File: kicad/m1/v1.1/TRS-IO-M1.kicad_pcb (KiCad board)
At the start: 2 copper layers, 117.5 x 104.8 mm, 26 parts, among them J1 Conn_02x20_Odd_Even, Q1 2N7000, Q2 2N7000, SW1 SW_Push, U1 HiLetgo-ESP-32S, U2 AS6C62256-PDIP, U3 MCP23S17_SP, U4 74LVC245, U5 74LVC245, U6 74LVC245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

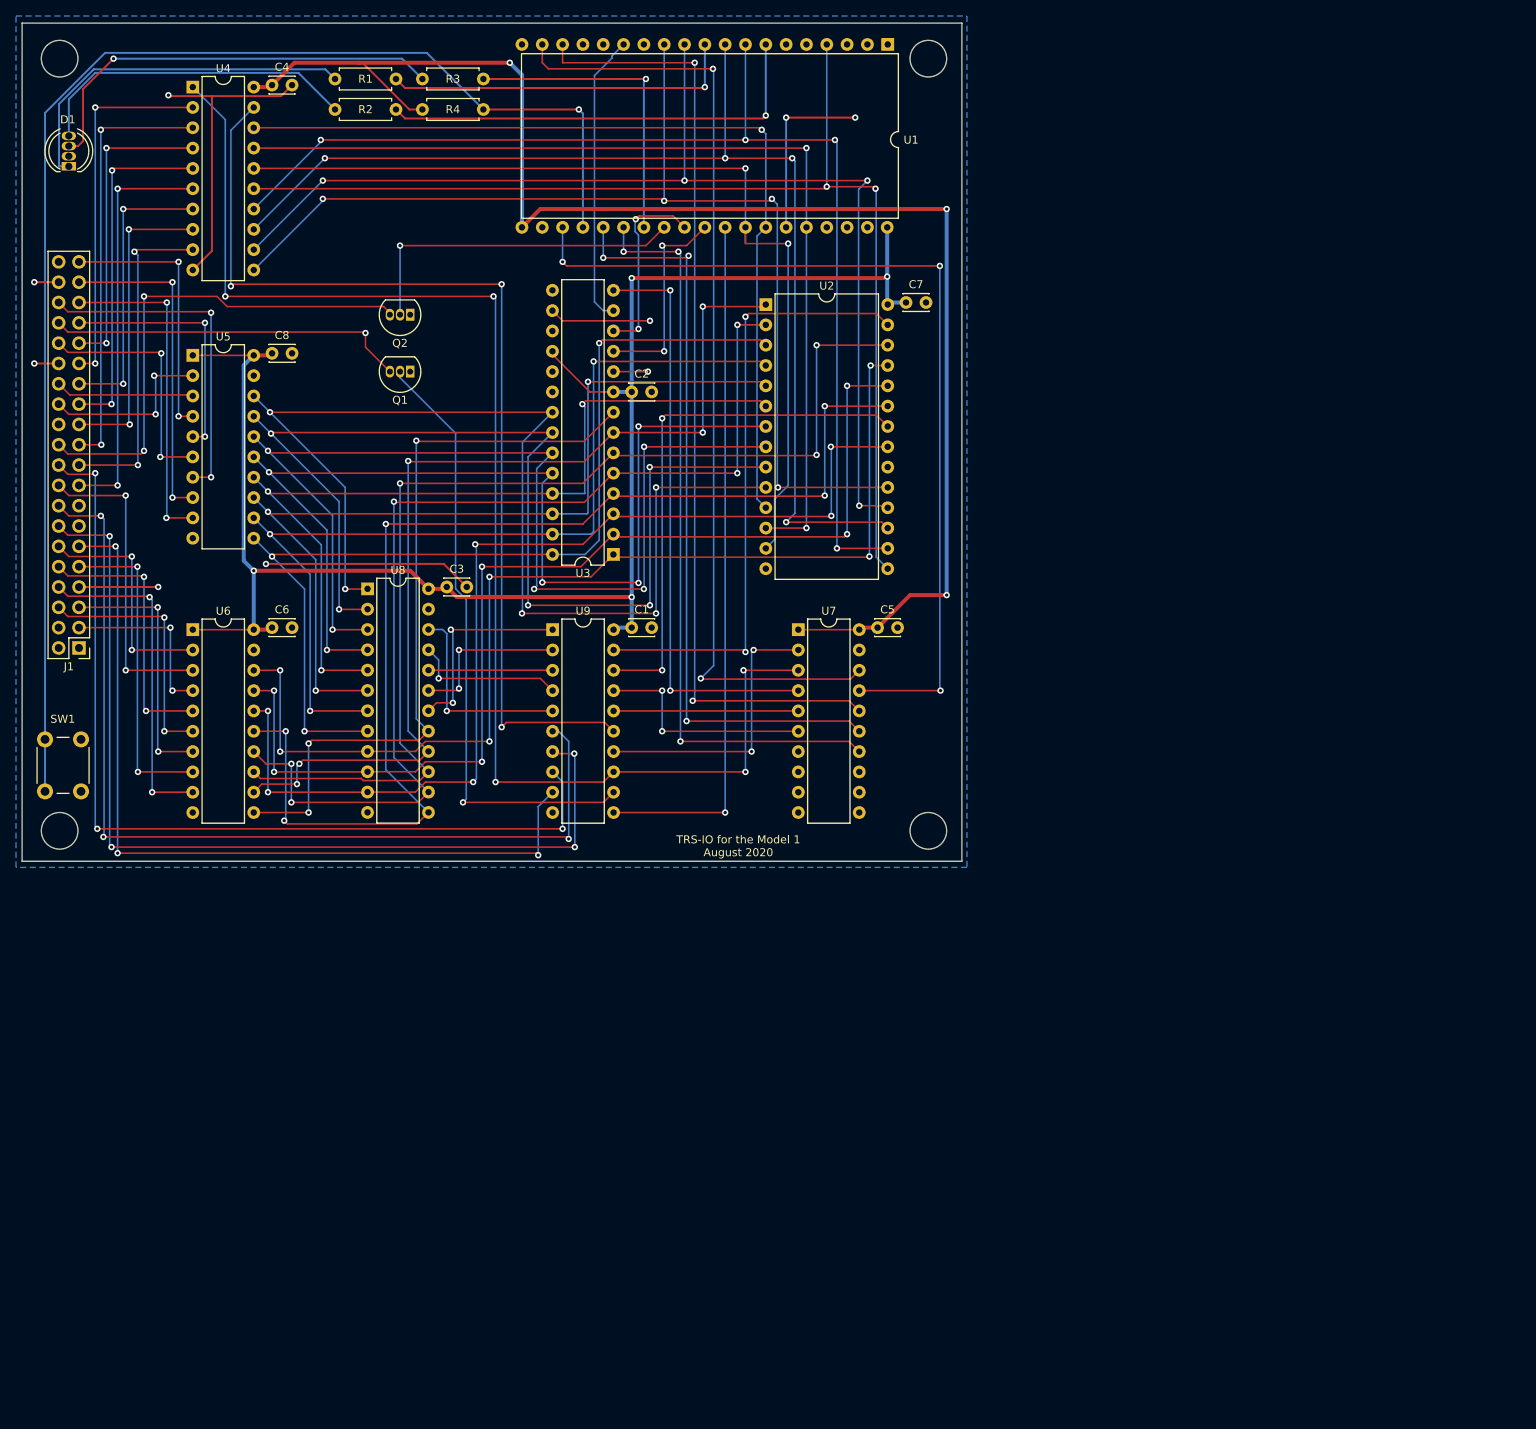
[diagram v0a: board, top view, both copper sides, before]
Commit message: Updates for TRS-IO-M1 v1.1
- Move data bus of the SRAM before the buffer
- added J2 for the edge connector
- Removed ADDR_2 and repurposed the connection for RAS*
- Move ESP_SEL_N to GPIO 27
- Move ESP_WAIT_RELEASE_N to GPIO 2
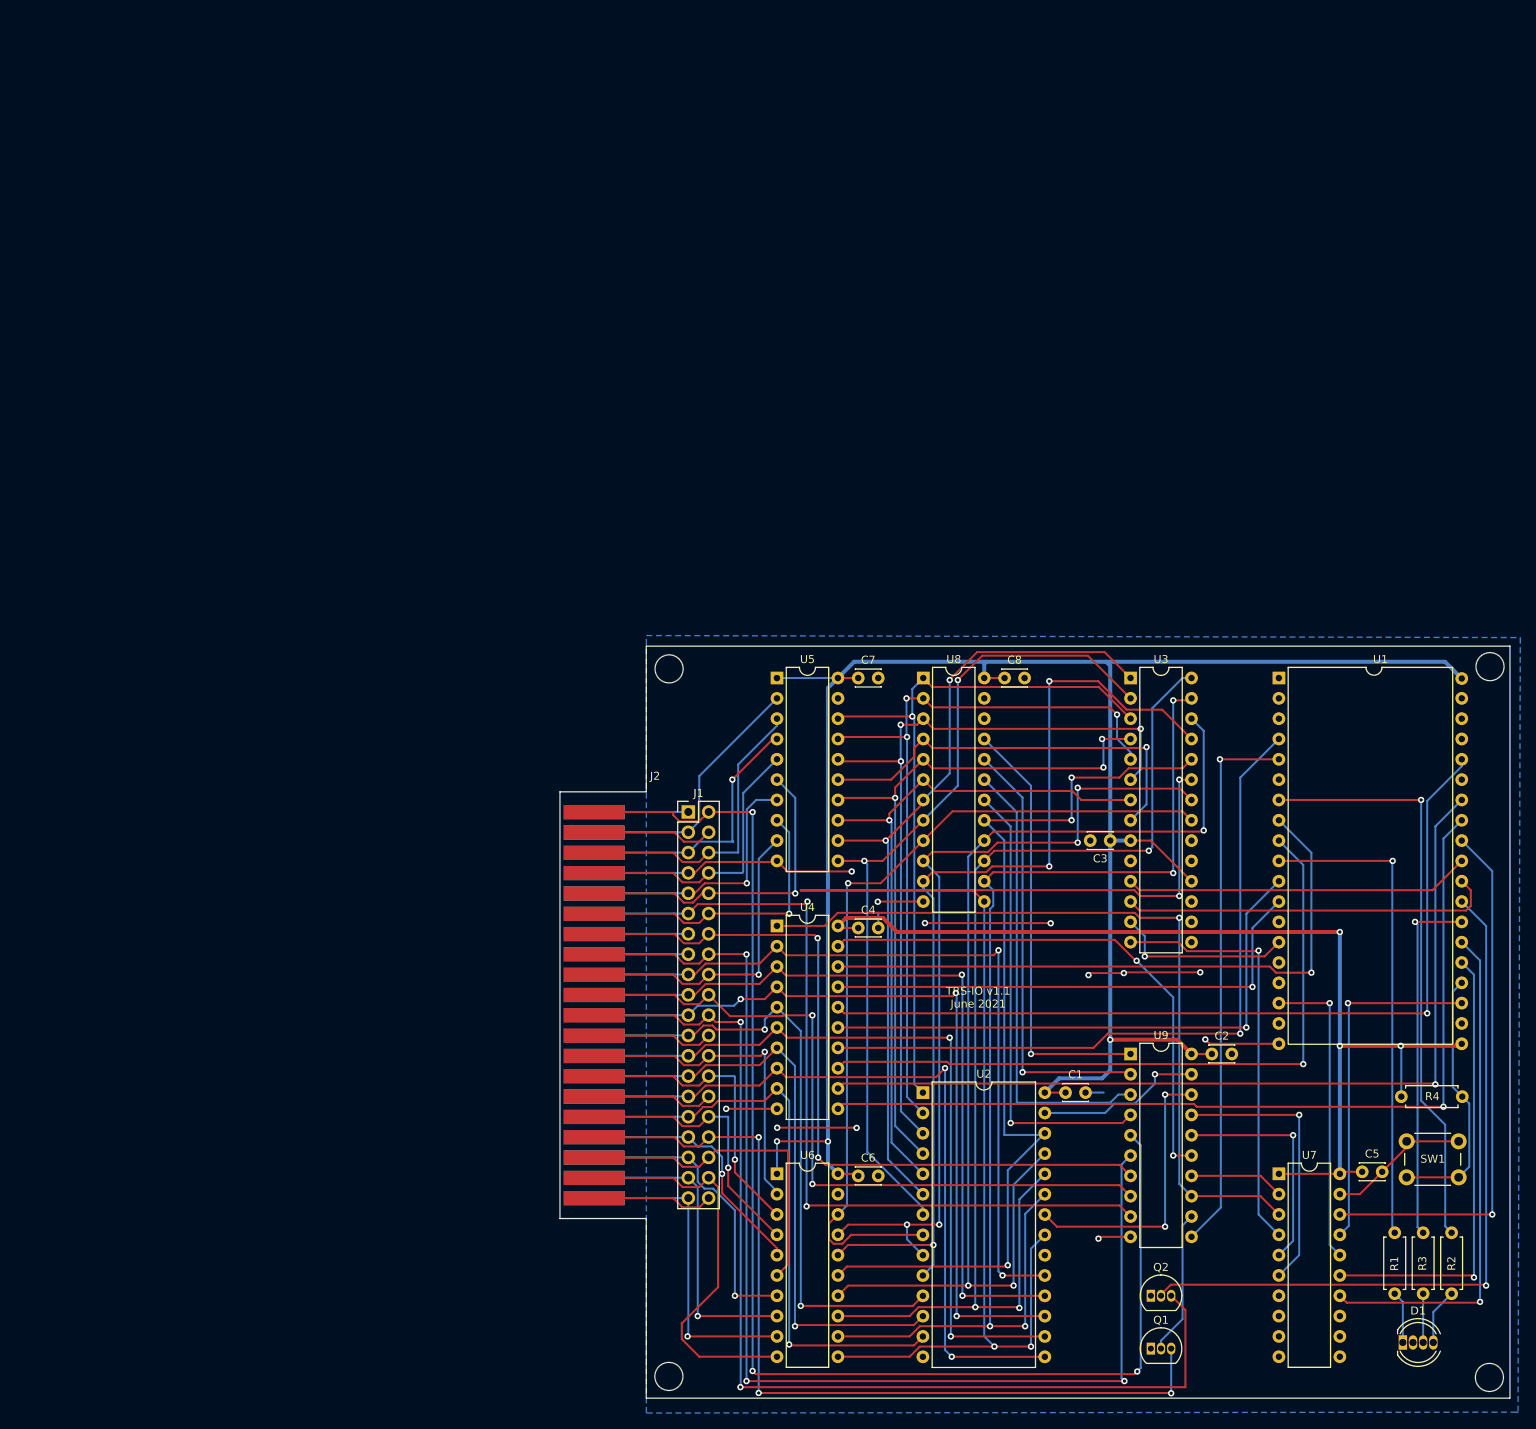
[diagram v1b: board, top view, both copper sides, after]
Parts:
- added J2: Conn_02x20_Odd_Even, TRS-IO-M1:TRSEDGE, F.Cu at (108.8, 92.8)
- moved D1 222.3 mm to (208.2, 135.1), turned to 0 degrees
- moved R2 192.7 mm to (214.2, 121.4), turned to 270 degrees
- moved R1 190.7 mm to (207.1, 121.4), turned to 270 degrees
- moved R3 186.0 mm to (210.7, 121.4), turned to 270 degrees
- moved R4 173.8 mm to (208.0, 104.3)
- moved SW1 173.2 mm to (208.6, 109.9), turned to 0 degrees
- moved Q2 153.7 mm to (176.7, 129.2), turned to 0 degrees
- moved Q1 153.3 mm to (176.7, 135.8), turned to 0 degrees
- moved C4 128.3 mm to (140.1, 83.3)
- moved U4 127.8 mm to (129.9, 83.0)
- moved C2 110.0 mm to (184.3, 99.0)
- moved U2 100.4 mm to (148.2, 103.8)
- moved C6 100.3 mm to (140.1, 114.2)
- moved C8 100.2 mm to (158.4, 52.0)
- moved U6 99.8 mm to (129.9, 114.0)
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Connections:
- U1 pad 18: ESP3_SEL_N -> Net-(U1-Pad18)
- U1 pad 30: ESP_WAIT_RELEASE_N -> ESP3_SEL_N
- U1 pad 5: Net-(U1-Pad5) -> ESP_WAIT_RELEASE_N
- U2 pad 1: AA14 -> AA10
- U2 pad 10: AA0 -> AA4
- U2 pad 11: DD0 -> D6
- U2 pad 12: DD1 -> D5
- U2 pad 13: DD2 -> D2
- U2 pad 15: DD3 -> D0
- U2 pad 16: DD4 -> D3
- U2 pad 17: DD5 -> D1
- U2 pad 18: DD6 -> D7
- U2 pad 19: DD7 -> D4
- U2 pad 21: AA10 -> AA2
- U2 pad 23: AA11 -> AA6
- U2 pad 24: AA9 -> AA7
- U2 pad 25: AA8 -> AA5
- U2 pad 26: AA13 -> AA3
- U2 pad 3: AA7 -> AA13
- U2 pad 4: AA6 -> AA11
- U2 pad 5: AA5 -> AA14
- U2 pad 6: AA4 -> AA8
- U2 pad 7: AA3 -> AA9
- U2 pad 8: AA2 -> AA0
- U4 pad 11: DD7 -> DD2
- U4 pad 12: DD6 -> DD0
- U4 pad 14: DD4 -> DD3
- U4 pad 15: DD3 -> DD6
- U4 pad 16: DD2 -> DD1
- U4 pad 17: DD1 -> DD7
- U4 pad 18: DD0 -> DD4
- U4 pad 2: D0 -> D4
- U4 pad 3: D1 -> D7
- U4 pad 4: D2 -> D1
- U4 pad 5: D3 -> D6
- U4 pad 6: D4 -> D3
- U4 pad 8: D6 -> D0
- U4 pad 9: D7 -> D2
- U5 pad 11: AA7 -> AA9
- U5 pad 12: AA6 -> AA8
- U5 pad 13: AA5 -> AA14
- U5 pad 14: AA4 -> AA11
- U5 pad 15: AA3 -> AA15
- U5 pad 16: AA2 -> AA13
- U5 pad 17: AA1 -> AA12
- U5 pad 18: AA0 -> AA10
- U5 pad 2: A0 -> A10
- U5 pad 3: A1 -> A12
- U5 pad 4: A2 -> A13
- U5 pad 5: A3 -> A15
- U5 pad 6: A4 -> A11
- U5 pad 7: A5 -> A14
- U5 pad 8: A6 -> A8
- U5 pad 9: A7 -> A9
- U6 pad 11: AA15 -> AA2
- U6 pad 12: AA14 -> AA6
- U6 pad 13: AA13 -> AA7
- U6 pad 14: AA12 -> AA5
- U6 pad 15: AA11 -> AA3
- U6 pad 16: AA10 -> AA4
- U6 pad 17: AA9 -> AA1
- U6 pad 18: AA8 -> AA0
- U6 pad 2: A8 -> A0
- U6 pad 3: A9 -> A1
- U6 pad 4: A10 -> A4
- U6 pad 5: A11 -> A3
- U6 pad 6: A12 -> A5
- U6 pad 7: A13 -> A7
- U6 pad 8: A14 -> A6
- U6 pad 9: A15 -> A2
- U8 pad 1: AA0 -> AA10
- U8 pad 10: AA9 -> AA1
- U8 pad 11: AA10 -> AA4
- U8 pad 13: AA11 -> AA2
- U8 pad 14: AA12 -> AA6
- U8 pad 15: AA13 -> AA7
- U8 pad 16: AA14 -> AA5
- U8 pad 17: AA15 -> AA3
- U8 pad 18: ADDR_TRS_IO -> ADDR_1
- U8 pad 19: ADDR_FREHD -> ADDR_0
- U8 pad 2: AA1 -> AA12
- U8 pad 20: ADDR_0 -> ADDR_FREHD
- U8 pad 21: ADDR_1 -> ADDR_TRS_IO
- U8 pad 22: ADDR_2 -> Net-(U8-Pad22)
- U8 pad 3: AA2 -> AA13
- U8 pad 4: AA3 -> AA15
- U8 pad 5: AA4 -> AA11
- U8 pad 6: AA5 -> AA14
- U8 pad 7: AA6 -> AA8
- U8 pad 8: AA7 -> AA9
- U8 pad 9: AA8 -> AA0
- U9 pad 5: ADDR_2 -> RAS_N
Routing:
- net RAS_N: track 0.00 -> 169.6 mm, vias 0 -> 3
- net BUTTON: track 172.5 -> 32.7 mm, vias 1 -> 0
- net ESP_MISO: track 120.0 -> 38.4 mm, vias 2 -> 1
- net READ_N: track 173.6 -> 98.5 mm, vias 5 -> 1
- net DD7: track 138.5 -> 63.9 mm, vias 4 -> 1
- net ESP_READ_N: track 115.0 -> 43.7 mm, vias 3 -> 1
- net DD6: track 142.1 -> 71.0 mm, vias 4 -> 1
- net INT_N: track 63.3 -> 133.1 mm
- net GND: track 120.5 -> 186.8 mm, vias 9 -> 12
- net WAIT_N: track 45.0 -> 110.7 mm, vias 1 -> 3
- net DD4: track 145.8 -> 80.2 mm, vias 4 -> 1
- net DBUS_SEL_N: track 127.5 -> 67.3 mm, vias 3 -> 2
- net WAIT: track 76.8 -> 18.1 mm, vias 1 -> 0
- net +3V3: track 187.4 -> 129.0 mm
- net AA11: track 148.0 -> 89.6 mm, vias 5 -> 3
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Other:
- board size 117.5 x 104.8 mm -> 118.7 x 94 mm
- board text added: "TRS-IO v1.1 June 2021"
- board text removed: "TRS-IO for the Model 1 August 2020"
